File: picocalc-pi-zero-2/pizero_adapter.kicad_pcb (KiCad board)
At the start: 2 copper layers, 29 x 51.8 mm, 3 parts, among them J1 Conn_01x20, J2 Conn_01x20, J3 Conn_02x20_Odd_Even

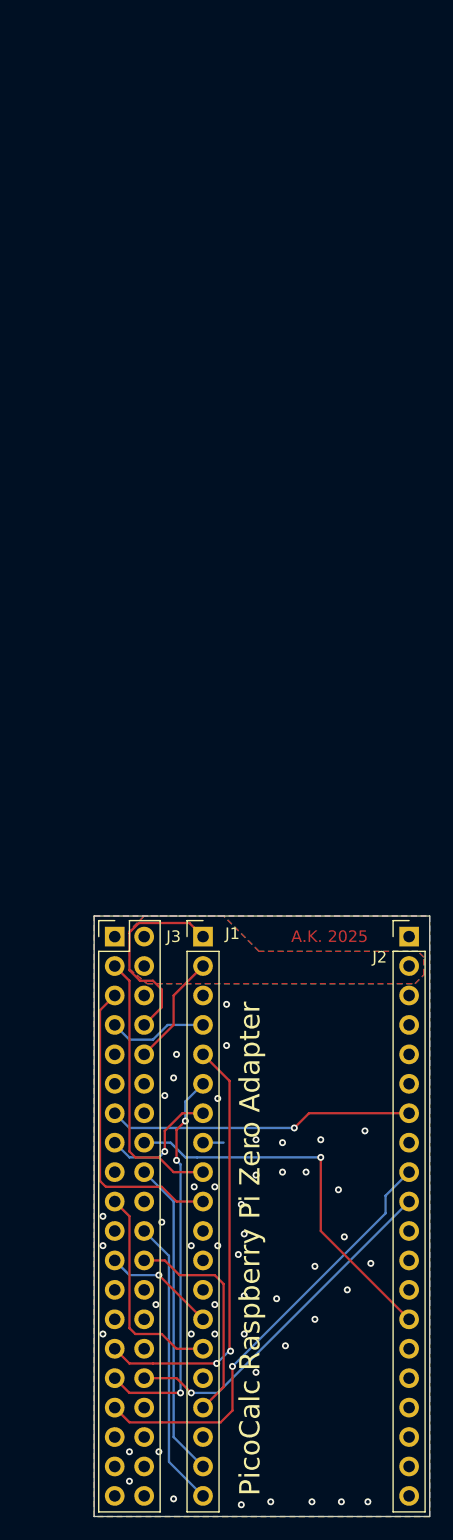
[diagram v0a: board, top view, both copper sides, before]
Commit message: picocalc-pi-zero-2: move rpi to clear the case
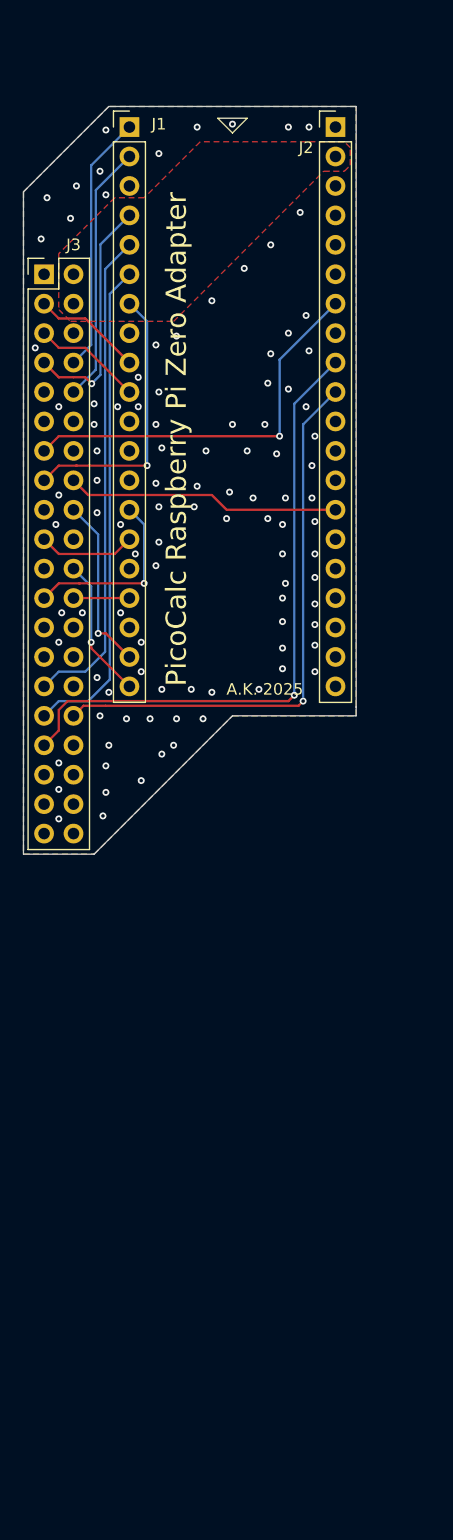
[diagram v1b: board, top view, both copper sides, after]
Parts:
- moved J1 70.1 mm to (95.2, 31.8)
- moved J2 70.1 mm to (113.0, 31.8)
- moved J3 57.5 mm to (87.9, 44.5)
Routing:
- net /PWM_L: track 30.2 -> 48.2 mm
- net /I2C1_SCL: track 26.2 -> 9.47 mm
- net /PWM_R: track 38.0 -> 54.6 mm
- net /~{SPI1_CS}: track 19.1 -> 4.83 mm
- net /I2C1_SDA: track 23.6 -> 9.47 mm
- net /GP5: track 10.8 -> 24.0 mm
- net /LCD_RST: track 25.0 -> 12.2 mm, vias 0 -> 1
- net /UART0_RX: track 9.72 -> 22.3 mm
- net /LCD_DC: track 27.5 -> 15.1 mm, vias 0 -> 1
- net /GP2: track 8.67 -> 20.7 mm, vias 0 -> 1
- net /SPI1_TX: track 18.5 -> 8.42 mm
- net /GP21: track 32.9 -> 23.7 mm, vias 1 -> 0
- net /GP4: track 34.0 -> 42.6 mm, vias 3 -> 0
- net /GP28: track 26.5 -> 34.3 mm
- net /SPI1_SCK: track 9.72 -> 16.0 mm
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- removed copper zone on B.Cu, net /VSYS
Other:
- board size 29 x 51.8 mm -> 28.7 x 64.5 mm
